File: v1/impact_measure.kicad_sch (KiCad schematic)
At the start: 63 parts, among them Q2 SP2002KNC, SW1 SW_Push, SW2 SW_Push, U2 ESP32-C3FH4, U3 GS2019-33TR5, U4 ADXL375BCCZ, Y1 40MHz

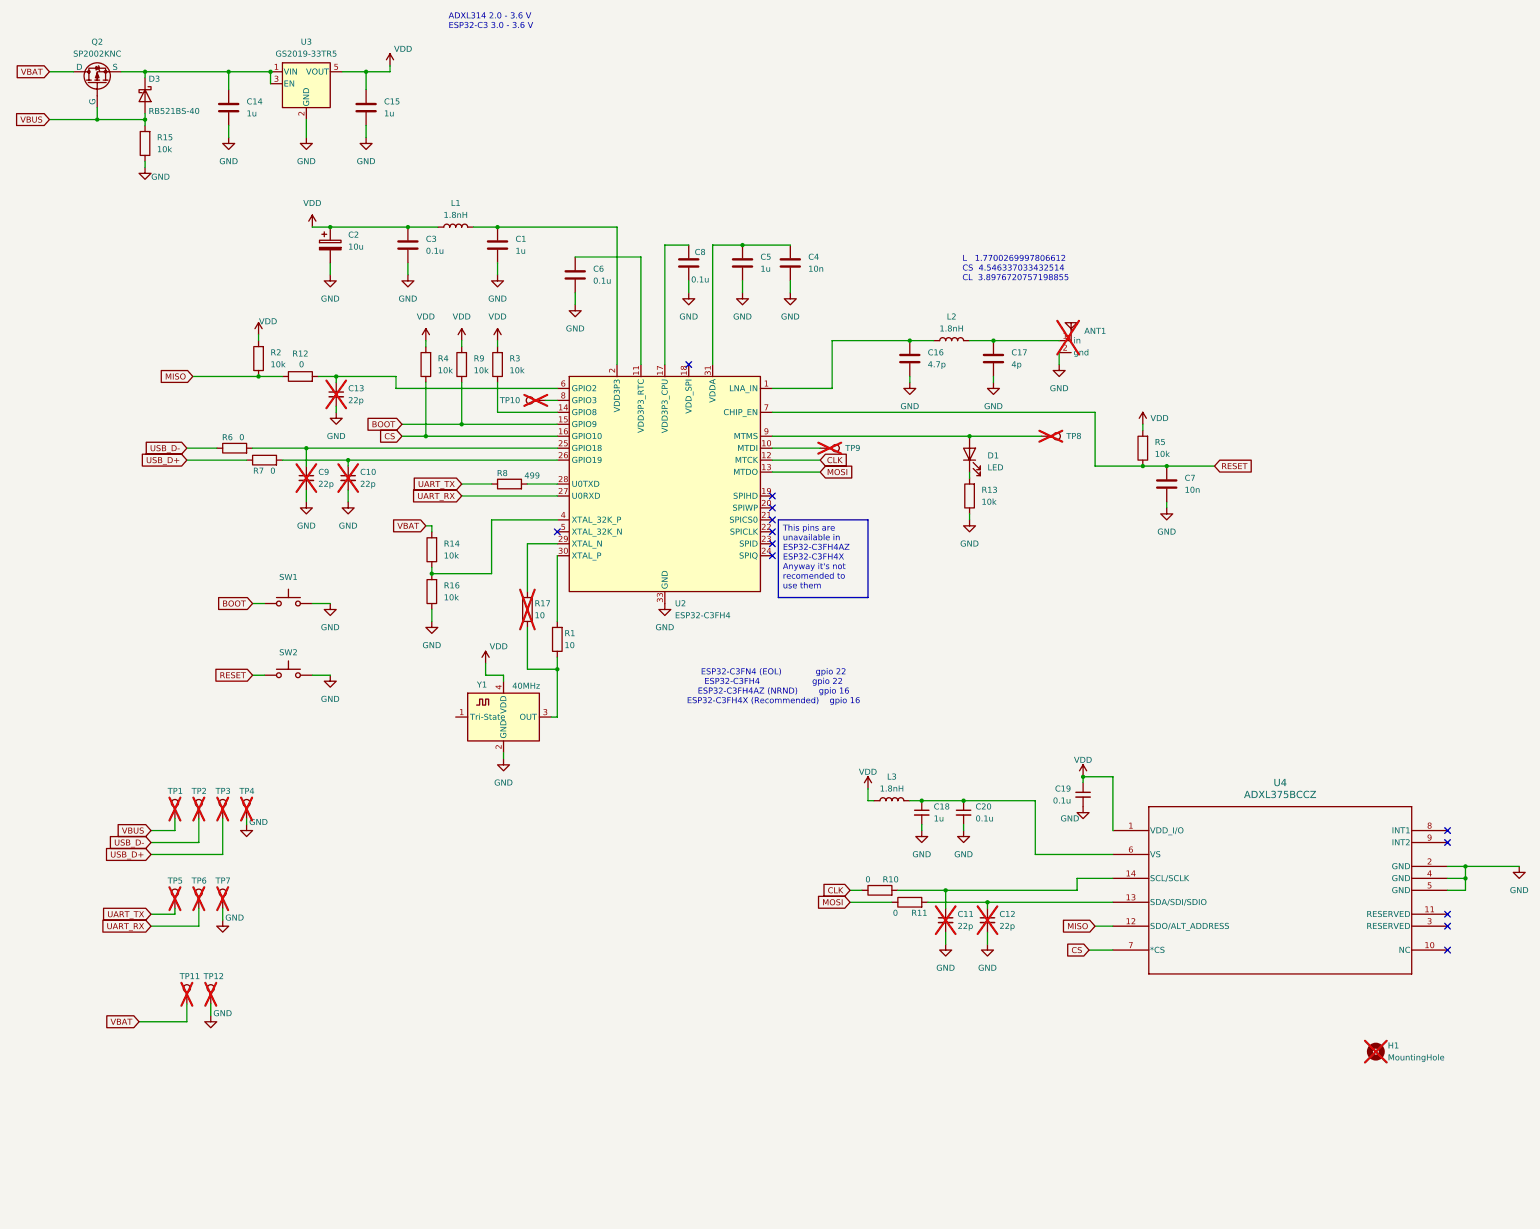
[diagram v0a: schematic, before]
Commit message: add decap to Y1 quarz change C2 electrolyte to ceramic add signals int1 and int2
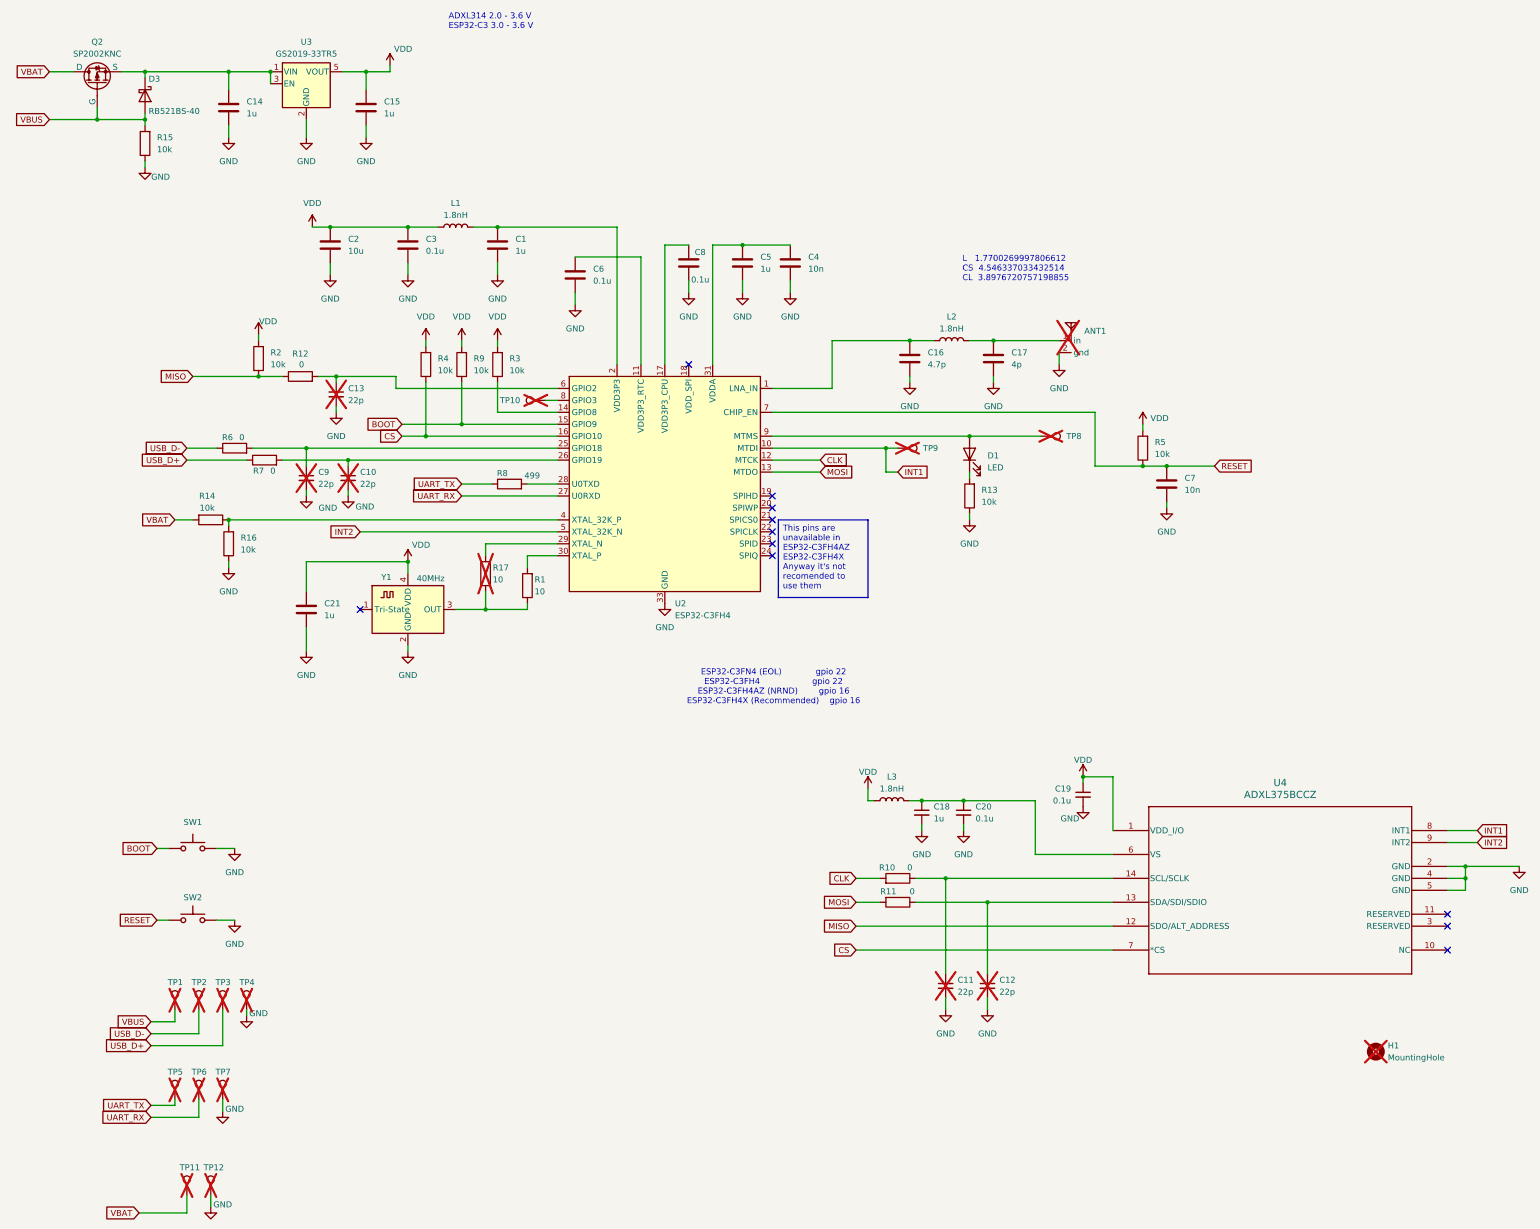
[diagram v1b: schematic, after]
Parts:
- removed C2: 10u, Capacitor_SMD:CP_Elec_4x5.4, symbol Device:C_Polarized
- added C2: 10u, Capacitor_SMD:C_0603_1608Metric, symbol Device:C
- added C21: 1u, Capacitor_SMD:C_0402_1005Metric, symbol Device:C
- U4: footprint LGA_CC-14-1_ADI -> Local:LGA_CC-14-1_ADI
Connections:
- net CLK: now also R10.2; no longer R10.1
- net GND: now also C2.2, C21.2
- net MOSI: now also R11.2; no longer R11.1
- net VDD: now also C2.1, C21.1
- net at C11.1, U4.14 (SCL/SCLK): now also R10.1; no longer R10.2
- net at C12.1, U4.13 (SDA/SDI/SDIO): now also R11.1; no longer R11.2
- net INT1: now reaches U4.8 (INT1)
- net INT1: now also TP9.1, U2.10 (MTDI)
- net INT2: now reaches U4.9 (INT2)
- net INT2: now also U2.5 (XTAL_32K_N)
- no-connect marks 13 -> 11
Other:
- moved on the sheet: C11, C12, R1, R10, R11, R14, R16, R17, SW1, SW2, TP1, TP11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

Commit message: fixed accel land pattern add via fetching increased m3 keepout diameter add int1 and int2 routes fixed wifi track width to 0,35mm moved 10u decap next to ESP32
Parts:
- U4: footprint Local:LGA_CC-14-1_ADI -> Local:LGA_CC-14-1_ADXL375
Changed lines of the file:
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@@
 			)
 		)
-		(property "Footprint" "Local:LGA_CC-14-1_ADI"
+		(property "Footprint" "Local:LGA_CC-14-1_ADXL375"
 			(at 250.19 191.77 0)
 			(effects

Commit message: fixed LCSC partnumbers fixed after DRC
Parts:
- ANT1, C10, C11, C12, C13, C9, R17, TP1, TP10, TP11, TP12, TP2, TP3, TP4, TP5, TP6, TP7, TP8, TP9: now left out of the parts list
- C2: LCSC C106254 -> C109453
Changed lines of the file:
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@@
 		(unit 1)
 		(exclude_from_sim no)
-		(in_bom yes)
+		(in_bom no)
 		(on_board yes)
 		(dnp yes)
@@
 		(unit 1)
 		(exclude_from_sim no)
-		(in_bom yes)
+		(in_bom no)
 		(on_board yes)
 		(dnp yes)
@@
 		(unit 1)
 		(exclude_from_sim no)
-		(in_bom yes)
+		(in_bom no)
 		(on_board yes)
 		(dnp yes)
@@
 		(unit 1)
 		(exclude_from_sim no)
-		(in_bom yes)
+		(in_bom no)
 		(on_board yes)
 		(dnp yes)
@@
 		(unit 1)
 		(exclude_from_sim no)
-		(in_bom yes)
+		(in_bom no)
 		(on_board yes)
 		(dnp yes)
@@
 		(unit 1)
 		(exclude_from_sim no)
-		(in_bom yes)
+		(in_bom no)
 		(on_board yes)
 		(dnp yes)
@@
 		(unit 1)
 		(exclude_from_sim no)
-		(in_bom yes)
+		(in_bom no)
 		(on_board yes)
 		(dnp yes)
@@
 		(unit 1)
 		(exclude_from_sim no)
-		(in_bom yes)
+		(in_bom no)
 		(on_board yes)
 		(dnp yes)
@@
 		(unit 1)
 		(exclude_from_sim no)
-		(in_bom yes)
+		(in_bom no)
 		(on_board yes)
 		(dnp yes)
@@
 		(unit 1)
 		(exclude_from_sim no)
-		(in_bom yes)
+		(in_bom no)
 		(on_board yes)
 		(dnp yes)
@@
 		(unit 1)
 		(exclude_from_sim no)
-		(in_bom yes)
+		(in_bom no)
 		(on_board yes)
 		(dnp yes)
@@
 		(unit 1)
 		(exclude_from_sim no)
-		(in_bom yes)
+		(in_bom no)
 		(on_board yes)
 		(dnp yes)
@@
 		(unit 1)
 		(exclude_from_sim no)
-		(in_bom yes)
+		(in_bom no)
 		(on_board yes)
 		(dnp yes)
@@
 		(unit 1)
 		(exclude_from_sim no)
-		(in_bom yes)
+		(in_bom no)
 		(on_board yes)
 		(dnp yes)
@@
 		(unit 1)
 		(exclude_from_sim no)
-		(in_bom yes)
+		(in_bom no)
 		(on_board yes)
 		(dnp yes)
@@
 		(unit 1)
 		(exclude_from_sim no)
-		(in_bom yes)
+		(in_bom no)
 		(on_board yes)
 		(dnp yes)
@@
 			)
 		)
-		(property "LCSC" "C106254"
+		(property "LCSC" "C109453"
 			(at 83.82 67.31 0)
 			(effects
@@
 		(unit 1)
 		(exclude_from_sim no)
-		(in_bom yes)
+		(in_bom no)
 		(on_board yes)
 		(dnp yes)
@@
 		(unit 1)
 		(exclude_from_sim no)
-		(in_bom yes)
+		(in_bom no)
 		(on_board yes)
 		(dnp yes)
@@
 		(unit 1)
 		(exclude_from_sim no)
-		(in_bom yes)
+		(in_bom no)
 		(on_board yes)
 		(dnp yes)

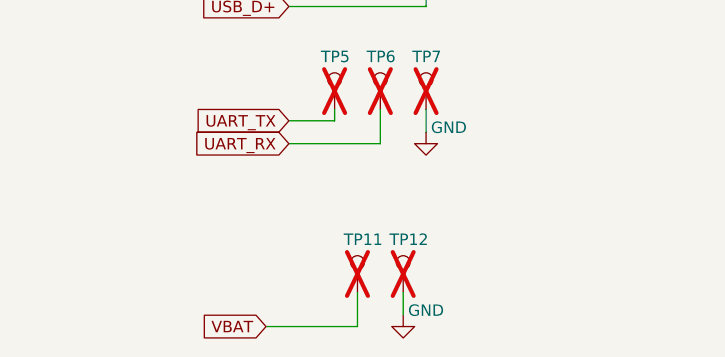
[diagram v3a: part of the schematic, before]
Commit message: added connector for battery
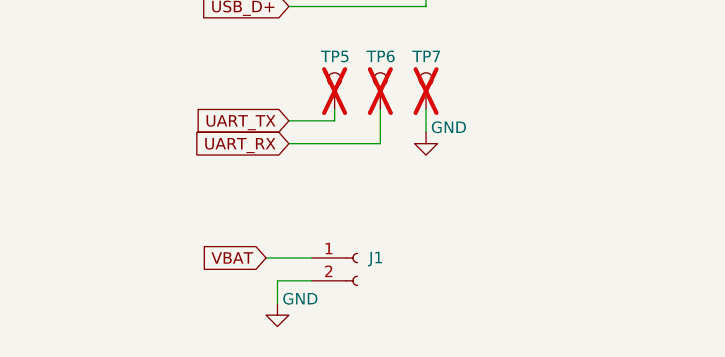
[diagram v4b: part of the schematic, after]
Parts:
- removed TP11, TP12: TestPoint, Local:TP_1x2mm, symbol Connector:TestPoint
- added J1: Bossie BX-MX1.25-2PWT, Local:mx1.25, symbol Connector:Conn_01x02_Socket
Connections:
- net GND: now also J1.2 (Pin_2)
- net VBAT: now also J1.1 (Pin_1)
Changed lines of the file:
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@@
 	(wire
 		(pts
-			(xy 58.42 269.24) (xy 58.42 271.78)
+			(xy 44.45 267.97) (xy 44.45 270.51)
 		)
 		(stroke
@@
 	(wire
 		(pts
-			(xy 53.34 269.24) (xy 53.34 273.05)
-		)
-		(stroke
-			(width 0)
-			(type default)
-		)
-	)
-	(wire
-		(pts
 			(xy 177.8 115.57) (xy 187.96 115.57)
 		)
@@
 	(wire
 		(pts
+			(xy 44.45 267.97) (xy 48.26 267.97)
+		)
+		(stroke
+			(width 0)
+			(type default)
+		)
+	)
+	(wire
+		(pts
 			(xy 60.96 248.92) (xy 60.96 251.46)
 		)
@@
 	(wire
 		(pts
-			(xy 43.18 273.05) (xy 53.34 273.05)
+			(xy 43.18 265.43) (xy 48.26 265.43)
 		)
 		(stroke
@@
 	(global_label "VBAT"
 		(shape input)
-		(at 43.18 273.05 180)
+		(at 43.18 265.43 180)
 		(fields_autoplaced yes)
 		(effects
@@
 		)
 		(property "Intersheetrefs" "${INTERSHEET_REFS}"
-			(at 35.78 273.05 0)
+			(at 35.78 265.43 0)
 			(effects
 				(font
@@
 	)
 	(symbol
+		(lib_id "Connector:Conn_01x02_Socket")
+		(at 53.34 265.43 0)
+		(unit 1)
+		(exclude_from_sim no)
+		(in_bom yes)
+		(on_board yes)
+		(dnp no)
+		(fields_autoplaced yes)
+		(property "Reference" "J1"
+			(at 54.61 265.4299 0)
+			(effects
+				(font
+					(size 1.27 1.27)
+				)
+				(justify left)
+			)
+		)
+		(property "Value" "Bossie BX-MX1.25-2PWT"
+			(at 54.61 267.9699 0)
+			(effects
+				(font
+					(size 1.27 1.27)
+				)
+				(justify left)
+				(hide yes)
+			)
+		)
+		(property "Footprint" "Local:mx1.25"
+			(at 53.34 265.43 0)
+			(effects
+				(font
+					(size 1.27 1.27)
+				)
+				(hide yes)
+			)
+		)
+		(property "Datasheet" "~"
+			(at 53.34 265.43 0)
+			(effects
+				(font
+					(size 1.27 1.27)
+				)
+				(hide yes)
+			)
+		)
+		(property "Description" "Generic connector, single row, 01x02, script generated"
+			(at 53.34 265.43 0)
+			(effects
+				(font
+					(size 1.27 1.27)
+				)
+				(hide yes)
+			)
+		)
+		(property "LCSC" "C18077932"
+			(at 53.34 265.43 0)
+			(effects
+				(font
+					(size 1.27 1.27)
+				)
+				(hide yes)
+			)
+		)
+		(pin "1"
+		)
+		(pin "2"
+		)
+		(instances
+			(project ""
+				(path "/e85e28eb-92fb-4c81-8f1d-062b0ba57fe6"
+					(reference "J1")
+					(unit 1)
+				)
+			)
+		)
+	)
+	(symbol
 		(lib_id "Device:C")
 		(at 261.62 118.11 0)
@@
 	(symbol
 		(lib_id "power:GND")
-		(at 58.42 271.78 0)
+		(at 44.45 270.51 0)
 		(unit 1)
 		(exclude_from_sim no)
@@
 		(dnp no)
 		(property "Reference" "#PWR039"
-			(at 58.42 278.13 0)
+			(at 44.45 276.86 0)
 			(effects
 				(font
@@
 		)
 		(property "Value" "GND"
-			(at 60.96 271.272 0)
+			(at 46.99 270.002 0)
 			(effects
 				(font
@@
 		)
 		(property "Footprint" ""
-			(at 58.42 271.78 0)
+			(at 44.45 270.51 0)
 			(effects
 				(font
@@
 		)
 		(property "Datasheet" ""
-			(at 58.42 271.78 0)
+			(at 44.45 270.51 0)
 			(effects
 				(font
@@
 		)
 		(property "Description" "Power symbol creates a global label with name \"GND\" , ground"
-			(at 58.42 271.78 0)
+			(at 44.45 270.51 0)
 			(effects
 				(font
@@
 	)
 	(symbol
-		(lib_id "Connector:TestPoint")
-		(at 58.42 269.24 0)
-		(unit 1)
-		(exclude_from_sim no)
-		(in_bom no)
-		(on_board yes)
-		(dnp yes)
-		(property "Reference" "TP12"
-			(at 56.896 263.398 0)
-			(effects
-				(font
-					(size 1.27 1.27)
-				)
-				(justify left)
-			)
-		)
-		(property "Value" "TestPoint"
-			(at 60.96 267.2079 0)
-			(effects
-				(font
-					(size 1.27 1.27)
-				)
-				(justify left)
-				(hide yes)
-			)
-		)
-		(property "Footprint" "Local:TP_1x2mm"
-			(at 63.5 269.24 0)
-			(effects
-				(font
-					(size 1.27 1.27)
-				)
-				(hide yes)
-			)
-		)
-		(property "Datasheet" "~"
-			(at 63.5 269.24 0)
-			(effects
-				(font
-					(size 1.27 1.27)
-				)
-				(hide yes)
-			)
-		)
-		(property "Description" "test point"
-			(at 58.42 269.24 0)
-			(effects
-				(font
-					(size 1.27 1.27)
-				)
-				(hide yes)
-			)
-		)
-		(property "LCSC" ""
-			(at 58.42 269.24 0)
-			(effects
-				(font
-					(size 1.27 1.27)
-				)
-				(hide yes)
-			)
-		)
-		(property "PartNumber" ""
-			(at 58.42 269.24 0)
-			(effects
-				(font
-					(size 1.27 1.27)
-				)
-				(hide yes)
-			)
-		)
-		(pin "1"
-		)
-		(instances
-			(project "impact_measure"
-				(path "/e85e28eb-92fb-4c81-8f1d-062b0ba57fe6"
-					(reference "TP12")
-					(unit 1)
-				)
-			)
-		)
-	)
-	(symbol
 		(lib_id "power:GND")
 		(at 261.62 123.19 0)
@@
 					(unit 1)
 				)
-			)
-		)
-	)
-	(symbol
-		(lib_id "Connector:TestPoint")
-		(at 53.34 269.24 0)
-		(unit 1)
-		(exclude_from_sim no)
-		(in_bom no)
-		(on_board yes)
-		(dnp yes)
-		(property "Reference" "TP11"
-			(at 51.816 263.398 0)
-			(effects
-				(font
-					(size 1.27 1.27)
-				)
-				(justify left)
-			)
-		)
-		(property "Value" "TestPoint"
-			(at 55.88 267.2079 0)
-			(effects
-				(font
-					(size 1.27 1.27)
-				)
-				(justify left)
-				(hide yes)
-			)
-		)
-		(property "Footprint" "Local:TP_1x2mm"
-			(at 58.42 269.24 0)
-			(effects
-				(font
-					(size 1.27 1.27)
-				)
-				(hide yes)
-			)
-		)
-		(property "Datasheet" "~"
-			(at 58.42 269.24 0)
-			(effects
-				(font
-					(size 1.27 1.27)
-				)
-				(hide yes)
-			)
-		)
-		(property "Description" "test point"
-			(at 53.34 269.24 0)
-			(effects
-				(font
-					(size 1.27 1.27)
-				)
-				(hide yes)
-			)
-		)
-		(property "LCSC" ""
-			(at 53.34 269.24 0)
-			(effects
-				(font
-					(size 1.27 1.27)
-				)
-				(hide yes)
-			)
-		)
-		(property "PartNumber" ""
-			(at 53.34 269.24 0)
-			(effects
-				(font
-					(size 1.27 1.27)
-				)
-				(hide yes)
-			)
-		)
-		(pin "1"
-		)
-		(instances
-			(project "impact_measure"
-				(path "/e85e28eb-92fb-4c81-8f1d-062b0ba57fe6"
-					(reference "TP11")
-					(unit 1)
-				)
